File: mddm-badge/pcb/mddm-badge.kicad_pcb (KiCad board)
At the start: 2 copper layers, 26.8 x 31.4 mm, 24 parts, among them J1 Conn_01x06, SW1 SKRKAEE020, U1 PIC10F322-IOT

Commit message: Work work work
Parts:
- removed REF** (x4): Tab, PCM_kikit:Tab

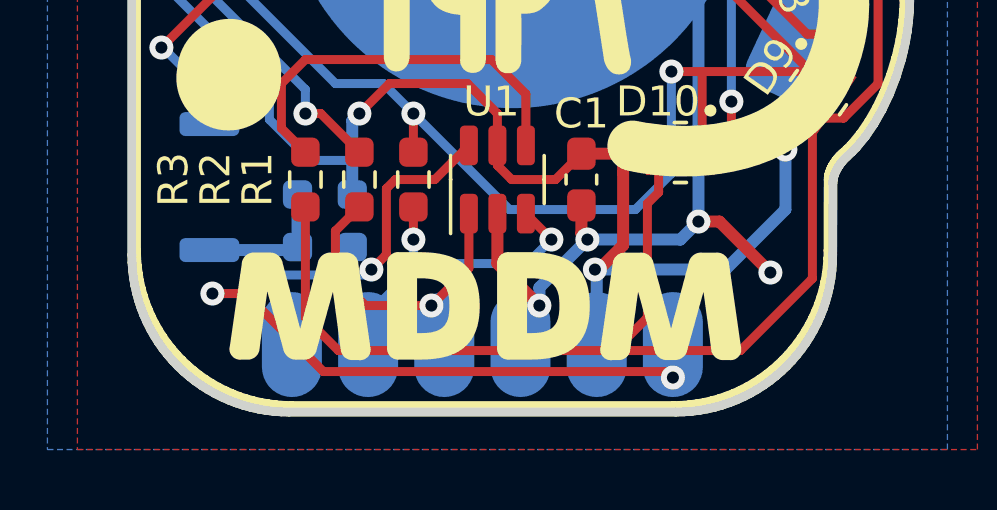
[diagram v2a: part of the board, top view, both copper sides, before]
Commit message: Bat modification
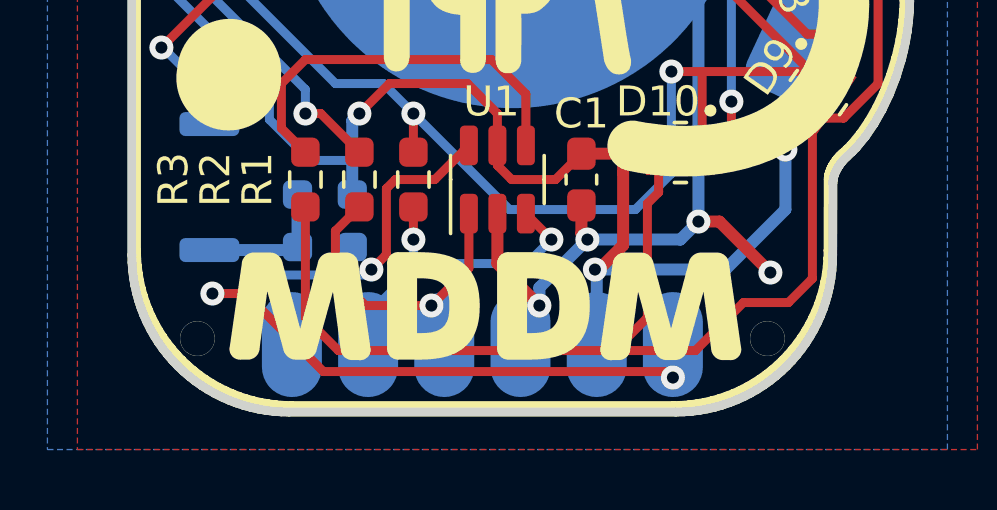
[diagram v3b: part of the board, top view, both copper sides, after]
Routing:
- net /blue: vias 0 -> 1
- net (no net): vias 0 -> 1
